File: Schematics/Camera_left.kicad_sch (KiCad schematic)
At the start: 8 parts, among them J1 Runcam Split 4 v2, U2 TPS22917DBVR

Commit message: assigned footprints ready for pcb design
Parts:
- C12, C13, C14, C15, J1: footprint (none) -> Capacitor_SMD:C_0805_2012Metric_Pad1.18x1.45mm_HandSolder
- R1, R2: footprint (none) -> Resistor_SMD:R_0805_2012Metric_Pad1.20x1.40mm_HandSolder
- U2: footprint SOT95P280X145-6N -> myFootprints:SOT95P280X145-6N
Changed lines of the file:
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@@
 			)
 		)
-		(property "Footprint" ""
+		(property "Footprint" "Capacitor_SMD:C_0805_2012Metric_Pad1.18x1.45mm_HandSolder"
 			(at 138.1252 97.79 0)
 			(effects
@@
 			)
 		)
-		(property "Footprint" ""
+		(property "Footprint" "Capacitor_SMD:C_0805_2012Metric_Pad1.18x1.45mm_HandSolder"
 			(at 69.5452 90.17 0)
 			(effects
@@
 			)
 		)
-		(property "Footprint" ""
+		(property "Footprint" "Capacitor_SMD:C_0805_2012Metric_Pad1.18x1.45mm_HandSolder"
 			(at 150.8252 97.79 0)
 			(effects
@@
 			)
 		)
-		(property "Footprint" ""
+		(property "Footprint" "Capacitor_SMD:C_0805_2012Metric_Pad1.18x1.45mm_HandSolder"
 			(at 227.33 93.98 0)
 			(effects
@@
 			)
 		)
-		(property "Footprint" ""
+		(property "Footprint" "Resistor_SMD:R_0805_2012Metric_Pad1.20x1.40mm_HandSolder"
 			(at 66.802 99.06 90)
 			(effects
@@
 			)
 		)
-		(property "Footprint" ""
+		(property "Footprint" "Capacitor_SMD:C_0805_2012Metric_Pad1.18x1.45mm_HandSolder"
 			(at 124.1552 97.79 0)
 			(effects
@@
 			)
 		)
-		(property "Footprint" "SOT95P280X145-6N"
+		(property "Footprint" "myFootprints:SOT95P280X145-6N"
 			(at 99.06 97.79 0)
 			(effects
@@
 			)
 		)
-		(property "Footprint" ""
+		(property "Footprint" "Resistor_SMD:R_0805_2012Metric_Pad1.20x1.40mm_HandSolder"
 			(at 201.422 86.36 90)
 			(effects

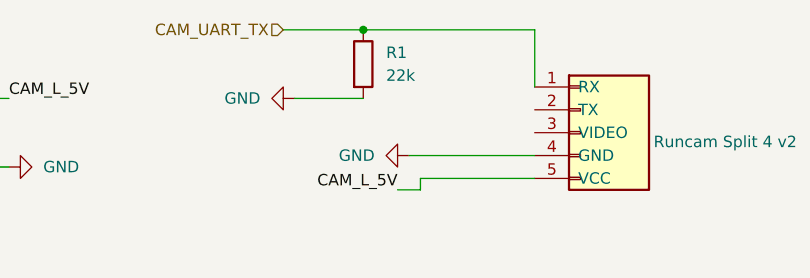
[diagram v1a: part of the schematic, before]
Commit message: Replaced LDO with smaller & Fixed resistor value for Camera tx lines
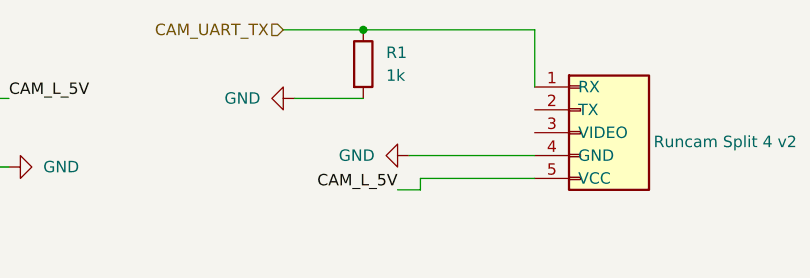
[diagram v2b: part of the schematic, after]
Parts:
- R1: value 22k -> 1k
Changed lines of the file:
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@@
 			)
 		)
-		(property "Value" "22k"
+		(property "Value" "1k"
 			(at 205.74 87.6299 0)
 			(effects

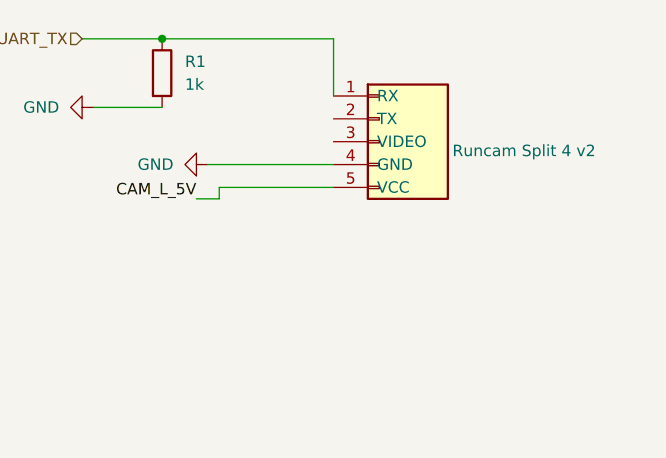
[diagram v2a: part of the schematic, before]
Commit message: Fixed Schematic and PCB refrences everything is connected correctly now
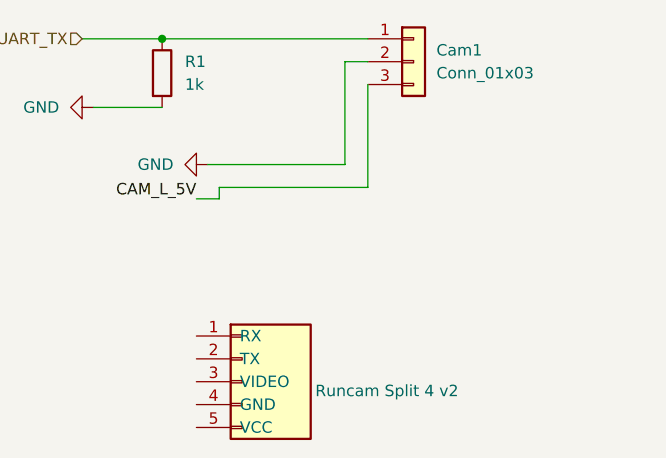
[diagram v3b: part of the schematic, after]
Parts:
- added Cam1: Conn_01x03, Connector_JST:JST_PH_B3B-PH-K_1x03_P2.00mm_Vertical, symbol Connector_Generic:Conn_01x03
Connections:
- net CAM_UART_TX: now also Cam1.1 (Pin_1); no longer J1.1 (RX)
- net GND: now also Cam1.2 (Pin_2); no longer J1.4 (GND)
- net at C13.1, C14.1, C15.1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: now also Cam1.3 (Pin_3); no longer J1.5 (VCC)
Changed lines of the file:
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@@
-	(wire
-		(pts
-			(xy 222.25 82.55) (xy 222.25 88.9)
-		)
-		(stroke
-			(width 0)
-			(type default)
-		)
-	)
 	(wire
 		(pts
@@
 	(wire
 		(pts
+			(xy 208.28 96.52) (xy 223.52 96.52)
+		)
+		(stroke
+			(width 0)
+			(type default)
+		)
+	)
+	(wire
+		(pts
 			(xy 68.58 95.25) (xy 83.82 95.25)
 		)
@@
 	(wire
 		(pts
-			(xy 209.55 99.06) (xy 222.25 99.06)
-		)
-		(stroke
-			(width 0)
-			(type default)
-		)
-	)
-	(wire
-		(pts
-			(xy 208.28 96.52) (xy 222.25 96.52)
-		)
-		(stroke
-			(width 0)
-			(type default)
-		)
-	)
-	(wire
-		(pts
-			(xy 203.2 82.55) (xy 222.25 82.55)
+			(xy 223.52 85.09) (xy 226.06 85.09)
+		)
+		(stroke
+			(width 0)
+			(type default)
+		)
+	)
+	(wire
+		(pts
+			(xy 203.2 82.55) (xy 226.06 82.55)
 		)
 		(stroke
@@
 	(wire
 		(pts
+			(xy 223.52 96.52) (xy 223.52 85.09)
+		)
+		(stroke
+			(width 0)
+			(type default)
+		)
+	)
+	(wire
+		(pts
 			(xy 149.86 97.79) (xy 163.83 97.79)
 		)
@@
 	(wire
 		(pts
+			(xy 226.06 99.06) (xy 226.06 87.63)
+		)
+		(stroke
+			(width 0)
+			(type default)
+		)
+	)
+	(wire
+		(pts
 			(xy 207.01 100.33) (xy 209.55 100.33)
+		)
+		(stroke
+			(width 0)
+			(type default)
+		)
+	)
+	(wire
+		(pts
+			(xy 209.55 99.06) (xy 226.06 99.06)
 		)
 		(stroke
@@
 	(symbol
 		(lib_id "Connector_Generic:Conn_01x05")
-		(at 227.33 93.98 0)
+		(at 212.09 120.65 0)
 		(unit 1)
 		(exclude_from_sim no)
@@
 		(fields_autoplaced yes)
 		(property "Reference" "J1"
-			(at 229.87 92.7099 0)
+			(at 214.63 119.3799 0)
 			(effects
 				(font
@@
 		)
 		(property "Value" "Runcam Split 4 v2"
-			(at 235.458 94.996 0)
+			(at 220.218 121.666 0)
 			(effects
 				(font
@@
 		)
 		(property "Footprint" "Capacitor_SMD:C_0805_2012Metric_Pad1.18x1.45mm_HandSolder"
-			(at 227.33 93.98 0)
+			(at 212.09 120.65 0)
 			(effects
 				(font
@@
 		)
 		(property "Datasheet" "~"
-			(at 227.33 93.98 0)
+			(at 212.09 120.65 0)
 			(effects
 				(font
@@
 		)
 		(property "Description" "Generic connector, single row, 01x05, script generated (kicad-library-utils/schlib/autogen/connector/)"
-			(at 226.314 83.058 0)
+			(at 211.074 109.728 0)
 			(effects
 				(font
@@
 					(unit 1)
 				)
+			)
+		)
+	)
+	(symbol
+		(lib_id "Connector_Generic:Conn_01x03")
+		(at 231.14 85.09 0)
+		(unit 1)
+		(exclude_from_sim no)
+		(in_bom yes)
+		(on_board yes)
+		(dnp no)
+		(fields_autoplaced yes)
+		(property "Reference" "Cam1"
+			(at 233.68 83.8199 0)
+			(effects
+				(font
+					(size 1.27 1.27)
+				)
+				(justify left)
+			)
+		)
+		(property "Value" "Conn_01x03"
+			(at 233.68 86.3599 0)
+			(effects
+				(font
+					(size 1.27 1.27)
+				)
+				(justify left)
+			)
+		)
+		(property "Footprint" "Connector_JST:JST_PH_B3B-PH-K_1x03_P2.00mm_Vertical"
+			(at 231.14 85.09 0)
+			(effects
+				(font
+					(size 1.27 1.27)
+				)
+				(hide yes)
+			)
+		)
+		(property "Datasheet" "~"
+			(at 231.14 85.09 0)
+			(effects
+				(font
+					(size 1.27 1.27)
+				)
+				(hide yes)
+			)
+		)
+		(property "Description" "Generic connector, single row, 01x03, script generated (kicad-library-utils/schlib/autogen/connector/)"
+			(at 231.14 85.09 0)
+			(effects
+				(font
+					(size 1.27 1.27)
+				)
+				(hide yes)
+			)
+		)
+		(pin "1"
+		)
+		(pin "2"
+		)
+		(pin "3"
+		)
+		(instances
+			(project ""
+				(path "/65068a32-f105-4204-b50e-234054c5a6d0/e8bd3566-d4f2-43cd-9088-441e27788299"
+					(reference "Cam1")
+					(unit 1)
+				)

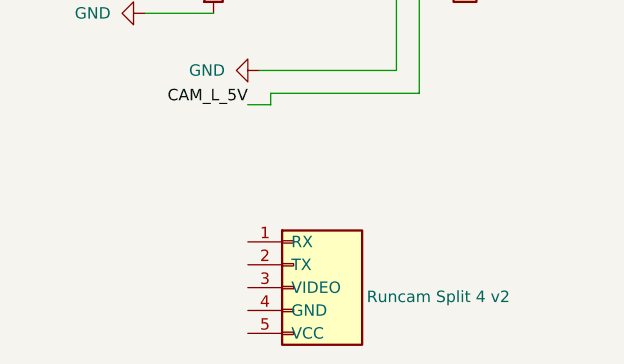
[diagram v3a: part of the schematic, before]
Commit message: fixed all refrences from shematic to pcb and added LED
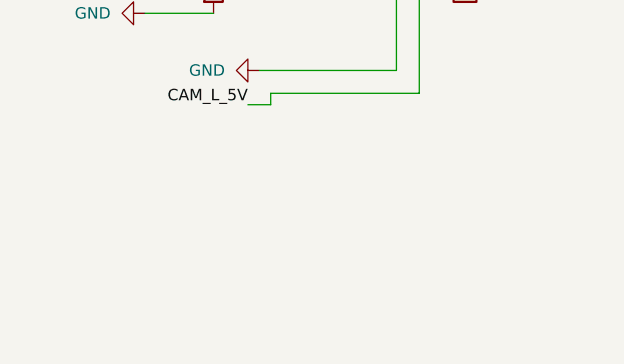
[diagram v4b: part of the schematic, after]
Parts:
- removed J1: Runcam Split 4 v2, Capacitor_SMD:C_0805_2012Metric_Pad1.18x1.45mm_HandSolder, symbol Connector_Generic:Conn_01x05
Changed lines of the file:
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@@
-	)
-	(symbol
-		(lib_id "Connector_Generic:Conn_01x05")
-		(at 212.09 120.65 0)
-		(unit 1)
-		(exclude_from_sim no)
-		(in_bom yes)
-		(on_board yes)
-		(dnp no)
-		(fields_autoplaced yes)
-		(property "Reference" "J1"
-			(at 214.63 119.3799 0)
-			(effects
-				(font
-					(size 1.27 1.27)
-				)
-				(justify left)
-				(hide yes)
-			)
-		)
-		(property "Value" "Runcam Split 4 v2"
-			(at 220.218 121.666 0)
-			(effects
-				(font
-					(size 1.27 1.27)
-				)
-				(justify left)
-			)
-		)
-		(property "Footprint" "Capacitor_SMD:C_0805_2012Metric_Pad1.18x1.45mm_HandSolder"
-			(at 212.09 120.65 0)
-			(effects
-				(font
-					(size 1.27 1.27)
-				)
-				(hide yes)
-			)
-		)
-		(property "Datasheet" "~"
-			(at 212.09 120.65 0)
-			(effects
-				(font
-					(size 1.27 1.27)
-				)
-				(hide yes)
-			)
-		)
-		(property "Description" "Generic connector, single row, 01x05, script generated (kicad-library-utils/schlib/autogen/connector/)"
-			(at 211.074 109.728 0)
-			(effects
-				(font
-					(size 1.27 1.27)
-				)
-				(hide yes)
-			)
-		)
-		(pin "5"
-		)
-		(pin "4"
-		)
-		(pin "3"
-		)
-		(pin "1"
-		)
-		(pin "2"
-		)
-		(instances
-			(project ""
-				(path "/65068a32-f105-4204-b50e-234054c5a6d0/e8bd3566-d4f2-43cd-9088-441e27788299"
-					(reference "J1")
-					(unit 1)
-				)
-			)
-		)
 	)
 	(symbol

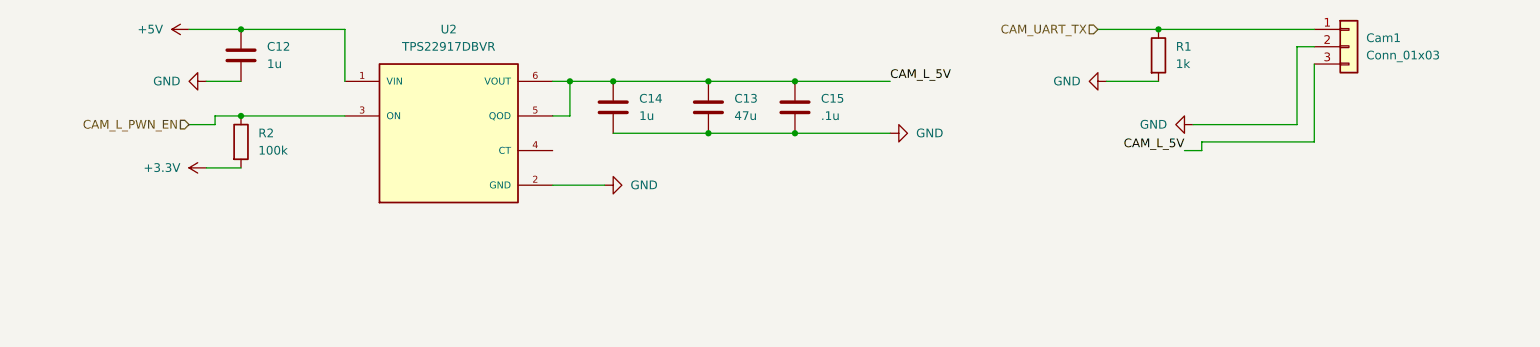
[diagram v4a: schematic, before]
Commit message: routing taking place only USB to do
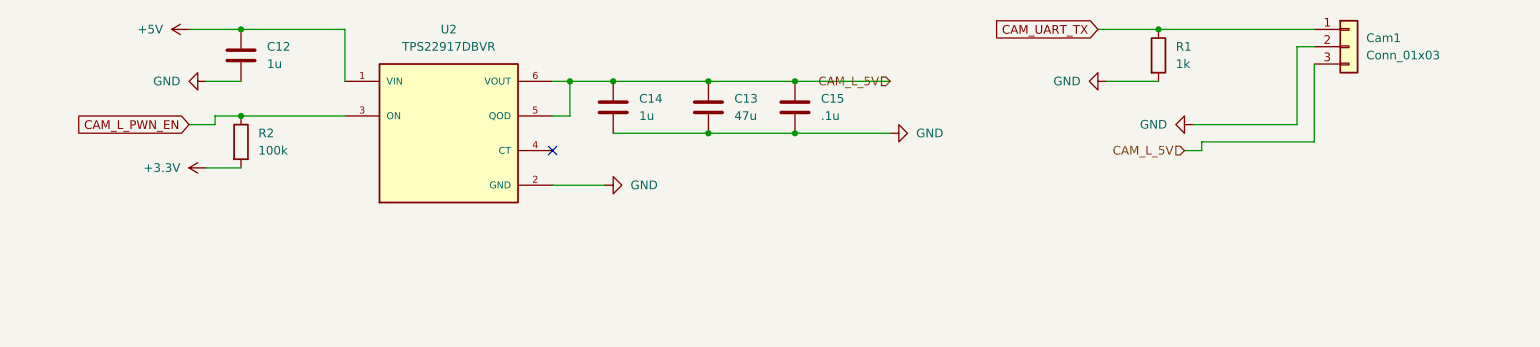
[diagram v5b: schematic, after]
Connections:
- net CAM_L_5V: now reaches C13.1, C14.1, C15.1, Cam1.3 (Pin_3), U2.5 (QOD), U2.6 (VOUT)
- no-connect marks 0 -> 1
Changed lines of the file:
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@@
 		(color 0 0 0 0)
 	)
+	(no_connect
+		(at 114.3 100.33)
+	)
 	(wire
 		(pts
@@
 			(width 0)
 			(type default)
-		)
-	)
-	(label "CAM_L_5V"
-		(at 163.83 90.17 0)
-		(effects
-			(font
-				(size 1.27 1.27)
-			)
-			(justify left bottom)
 		)
 	)
@@
 		)
 	)
-	(label "CAM_L_5V"
-		(at 207.01 100.33 180)
-		(effects
-			(font
-				(size 1.27 1.27)
-			)
-			(justify right bottom)
-		)
-	)
-	(hierarchical_label "CAM_L_PWN_EN"
+	(global_label "CAM_L_PWN_EN"
 		(shape input)
 		(at 60.96 96.52 180)
+		(fields_autoplaced yes)
 		(effects
 			(font
@@
 			(justify right)
 		)
-	)
-	(hierarchical_label "CAM_UART_TX"
+		(property "Intersheetrefs" "${INTERSHEET_REFS}"
+			(at 43.7025 96.52 0)
+			(effects
+				(font
+					(size 1.27 1.27)
+				)
+				(justify right)
+				(hide yes)
+			)
+		)
+	)
+	(global_label "CAM_UART_TX"
 		(shape input)
 		(at 194.31 82.55 180)
-		(effects
-			(font
+		(fields_autoplaced yes)
+		(effects
+			(font
+				(size 1.27 1.27)
+			)
+			(justify right)
+		)
+		(property "Intersheetrefs" "${INTERSHEET_REFS}"
+			(at 178.7458 82.55 0)
+			(effects
+				(font
+					(size 1.27 1.27)
+				)
+				(justify right)
+				(hide yes)
+			)
+		)
+	)
+	(hierarchical_label "CAM_L_5V"
+		(shape input)
+		(at 207.01 100.33 180)
+		(effects
+			(font
+				(size 1.27 1.27)
+			)
+			(justify right)
+		)
+	)
+	(hierarchical_label "CAM_L_5V"
+		(shape input)
+		(at 163.83 90.17 180)
+		(effects
+			(font

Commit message: Cleaned up schematic added ocilator added jtag 10 pin begining routing again
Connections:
- net CAM_L_5V: no longer names the net of C13.1, C14.1, C15.1, Cam1.3 (Pin_3), U2.5 (QOD), U2.6 (VOUT)
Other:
- moved on the sheet: C12, C13, C14, C15, Cam1, R1, R2, U2

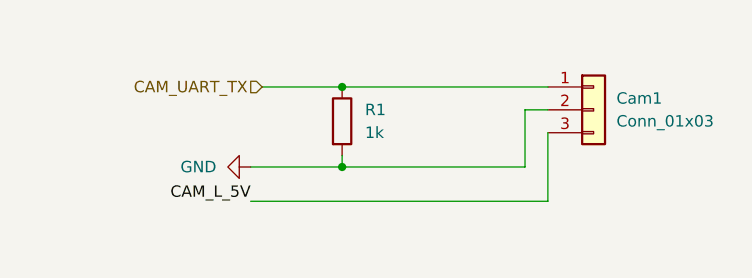
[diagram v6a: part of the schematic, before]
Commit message: second final draft finished routing added swd debug with stlink capabilities pending review for and data sheet review to ensure parts are correct, also need to edge cut ocillator
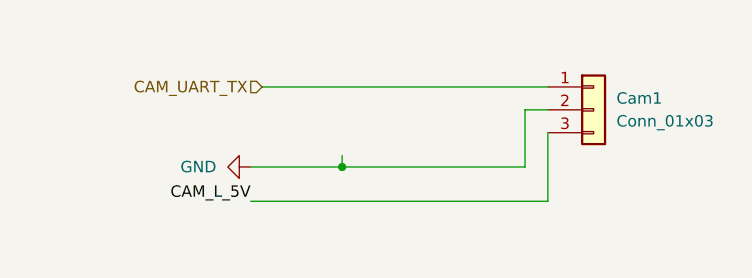
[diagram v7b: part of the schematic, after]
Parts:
- removed R1: 1k, Resistor_SMD:R_0805_2012Metric_Pad1.20x1.40mm_HandSolder, symbol Device:R
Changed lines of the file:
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@@
-	)
-	(junction
-		(at 203.2 88.9)
-		(diameter 0)
-		(color 0 0 0 0)
 	)
 	(junction
@@
 	(wire
 		(pts
-			(xy 203.2 88.9) (xy 226.06 88.9)
+			(xy 194.31 88.9) (xy 226.06 88.9)
 		)
 		(stroke
@@
 		(pts
 			(xy 203.2 97.79) (xy 203.2 96.52)
-		)
-		(stroke
-			(width 0)
-			(type default)
-		)
-	)
-	(wire
-		(pts
-			(xy 194.31 88.9) (xy 203.2 88.9)
 		)
 		(stroke
@@
 					(unit 1)
 				)
-			)
-		)
-	)
-	(symbol
-		(lib_id "Device:R")
-		(at 203.2 92.71 0)
-		(unit 1)
-		(exclude_from_sim no)
-		(in_bom yes)
-		(on_board yes)
-		(dnp no)
-		(fields_autoplaced yes)
-		(property "Reference" "R1"
-			(at 205.74 91.4399 0)
-			(effects
-				(font
-					(size 1.27 1.27)
-				)
-				(justify left)
-			)
-		)
-		(property "Value" "1k"
-			(at 205.74 93.9799 0)
-			(effects
-				(font
-					(size 1.27 1.27)
-				)
-				(justify left)
-			)
-		)
-		(property "Footprint" "Resistor_SMD:R_0805_2012Metric_Pad1.20x1.40mm_HandSolder"
-			(at 201.422 92.71 90)
-			(effects
-				(font
-					(size 1.27 1.27)
-				)
-				(hide yes)
-			)
-		)
-		(property "Datasheet" "~"
-			(at 203.2 92.71 0)
-			(effects
-				(font
-					(size 1.27 1.27)
-				)
-				(hide yes)
-			)
-		)
-		(property "Description" "Resistor"
-			(at 203.2 92.71 0)
-			(effects
-				(font
-					(size 1.27 1.27)
-				)
-				(hide yes)
-			)
-		)
-		(pin "2"
-		)
-		(pin "1"
-		)
-		(instances
-			(project ""
-				(path "/65068a32-f105-4204-b50e-234054c5a6d0/e8bd3566-d4f2-43cd-9088-441e27788299"
-					(reference "R1")
-					(unit 1)
-				)
